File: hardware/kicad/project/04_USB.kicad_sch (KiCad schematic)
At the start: 0 parts

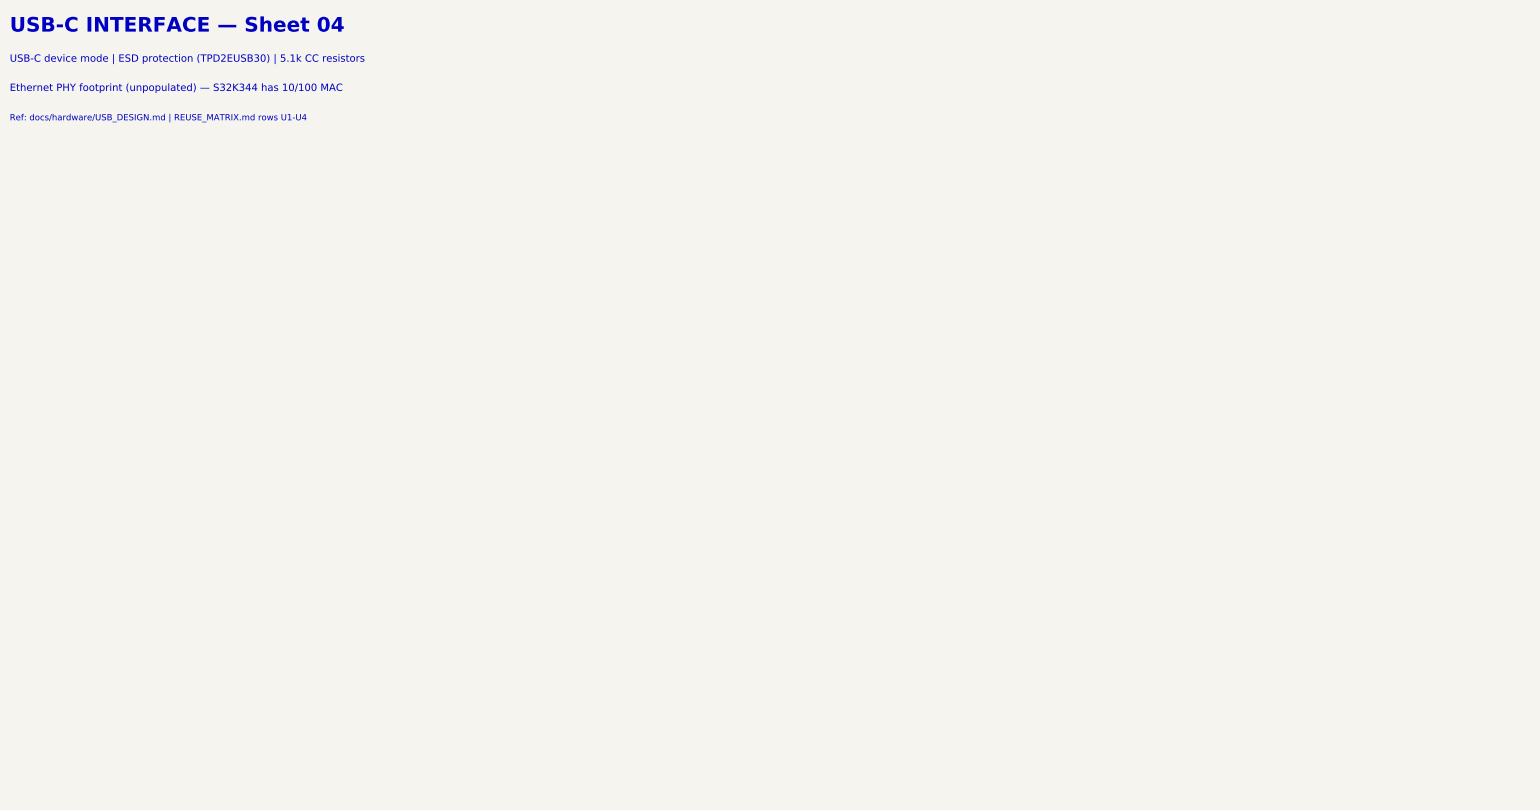
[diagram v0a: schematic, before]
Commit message: feat(hardware): TB-HW-002 — populate all 12 schematic sheets with components
Populated 235 component symbols across all 12 KiCad schematic sheets:
- 01_Power: Reverse polarity, TVS (SMCJ33A), buck (LMR33630), LDO (TPS7A1633), VREF (REF5050) — 30 symbols
- 02_MCU: S32K344 (6 units), clock (40MHz+32kHz), decoupling, reset, boot config, LEDs — 30 symbols
- 03_CAN: 4x TJA1043 with CM chokes (ACT45B-510), split termination, bus filter caps — 36 symbols
- 04_USB: Molex USB-C, TPD2EUSB30 ESD, CC resistors, eFuse, Ethernet PHY footprint — 9 symbols
- 05_Inputs: 8 analog channels (RC+clamp), 2x CJ125 WBO2, 2x TLE2072 knock amps — 50 symbols
- 06_Injectors: TLE8888-2QK (8-ch P&H), flyback diodes, current sense — 14 symbols
- 07_Ignition: 6x ISL9V3040S3 IGBTs with gate resistors (100R), pull-downs (10k) — 24 symbols
- 08_Outputs: DRV8873 ETC H-bridge, TLE8110ED low-side (boost+relays), BTS4140N tach — 12 symbols
- 09_Protection: TPS3850G33 watchdog, safe-state FET, ESD diodes (PESD5V0) — 14 symbols
- 10_Connectors: 42-pin Deutsch DTM (2 units), 2x CAN 4-pin, diagnostic 4-pin — 5 symbols
- 11_Programming: TC2050 SWD, 8 test points, production security notes — 11 symbols
- 00_Cover: Block diagram, BOM summary, spec references, revision history

Symbol library: 18 custom symbols with complete pin assignments
Components from COMPONENT_SELECTION.md r0.1
42-pin connector per INTERFACE_SPECIFICATION.md (authority)
All MCU pins per MCU_SELECTION.md pin allocation
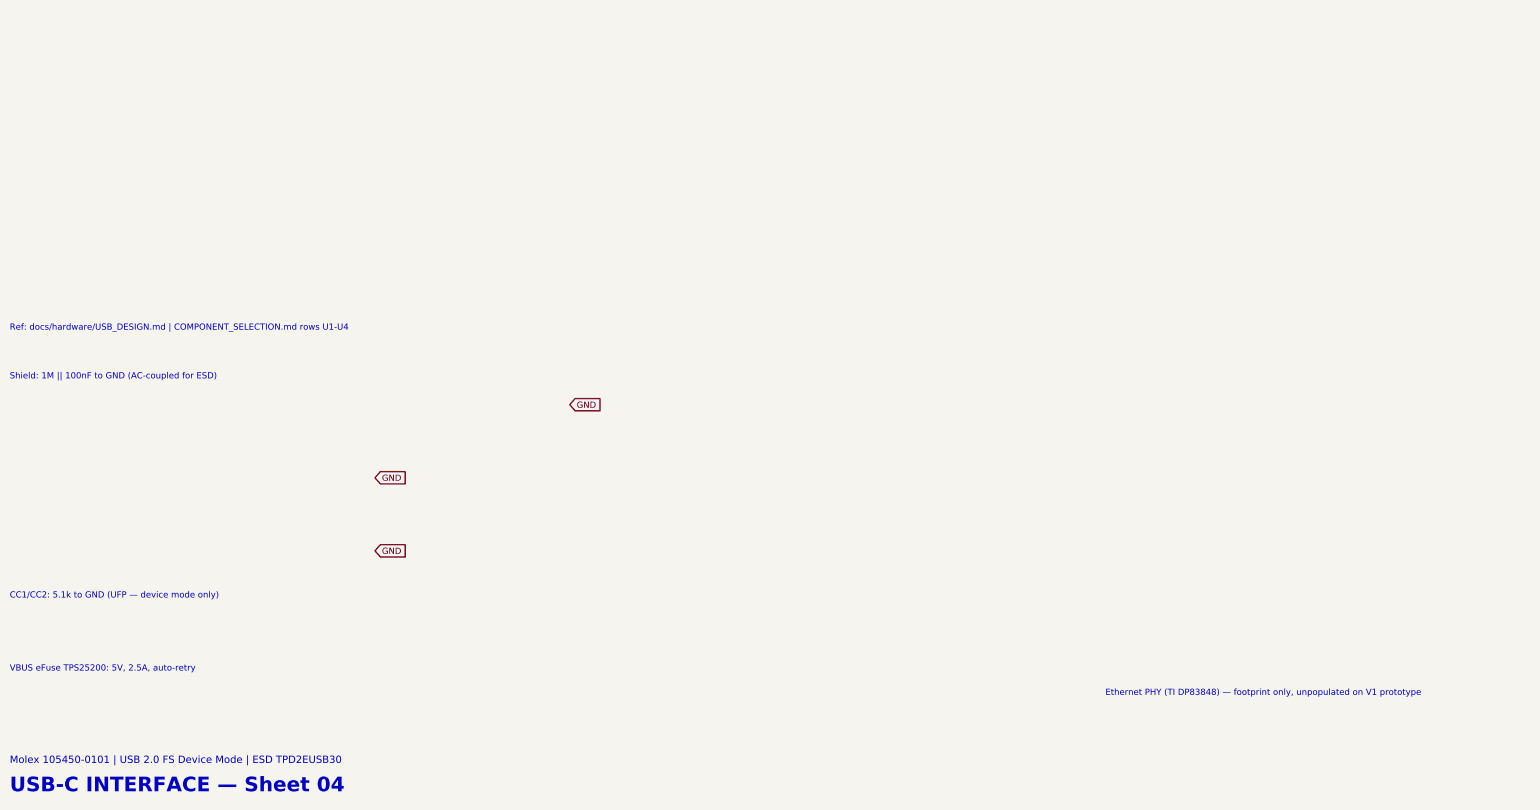
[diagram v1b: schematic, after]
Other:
- note added: "CC1/CC2: 5.1k to GND (UFP — device mode only)"
- note added: "Ethernet PHY (TI DP83848) — footprint only, unpopulated on V1 prototype"
- note added: "Molex 105450-0101 | USB 2.0 FS Device Mode | ESD TPD2EUSB30"
- note added: "Ref: docs/hardware/USB_DESIGN.md | COMPONENT_SELECTION.md rows U1-U4"
- note added: "Shield: 1M || 100nF to GND (AC-coupled for ESD)"
- note added: "VBUS eFuse TPS25200: 5V, 2.5A, auto-retry"
- note removed: "Ethernet PHY footprint (unpopulated) — S32K344 has 10/100 MAC"
- note removed: "Ref: docs/hardware/USB_DESIGN.md | REUSE_MATRIX.md rows U1-U4"
- note removed: "USB-C device mode | ESD protection (TPD2EUSB30) | 5.1k CC resistors"
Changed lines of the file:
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@@
-(kicad_sch (version 20240108) (generator "eeschema")
+(kicad_sch (version 20240108) (generator "7100CPT-schematic-gen")
   (paper "A3")
   (title_block
     (title "7100CPT ECU — USB-C Interface")
     (date "2026-07-03")
-    (rev "0.1")
+    (rev "0.2")
     (company "${COMPANY}")
-    (comment 1 "USB-C device, ESD (TPD2EUSB30), CC resistors, Ethernet PHY footprint (NP)")
+    (comment 1 "USB-C device, ESD, CC resistors, Ethernet PHY footprint (NP)")
     (comment 2 "NXP S32K344 | rusEFI Firmware | IPC Class 3")
     (comment 3 "High-Tg FR-4 (TG170+) | ENIG | 1.6 mm")
-    (comment 4 "REUSE_MATRIX.md — NXP Reference Following")
+    (comment 4 "Phase 0 Approved | REUSE_MATRIX gate passed")
     (comment 5 "-40C to +85C | IP67 Target | 6-Layer")
   )
-  (symbol_instances)
-  (text "USB-C INTERFACE — Sheet 04"
-    (at 25 24 0) (effects (font (size 3.0 3.0) bold) (justify left bottom)))
-  (text "USB-C device mode | ESD protection (TPD2EUSB30) | 5.1k CC resistors"
-    (at 25 30 0) (effects (font (size 1.5 1.5)) (justify left bottom)))
-  (text "Ethernet PHY footprint (unpopulated) — S32K344 has 10/100 MAC"
-    (at 25 36 0) (effects (font (size 1.5 1.5)) (justify left bottom)))
-  (text "Ref: docs/hardware/USB_DESIGN.md | REUSE_MATRIX.md rows U1-U4"
-    (at 25 42 0) (effects (font (size 1.27 1.27)) (justify left bottom)))
+  (symbol_instances
+  (symbol (lib_id "7100CPT:USB_C_MOLEX") (at 100 150 0) (unit 1)
+    (exclude_from_sim yes) (in_bom yes) (on_board yes) (dnp no)
+    (property "Reference" "J2" (at 100 150 0) (effects (font (size 1.27 1.27))))
+    (property "Value" "105450-0101" (at 100 143.65 0) (effects (font (size 1.27 1.27))))
+  )
+  (symbol (lib_id "7100CPT:TPD2EUSB30") (at 150 150 0) (unit 1)
+    (exclude_from_sim yes) (in_bom yes) (on_board yes) (dnp no)
+    (property "Reference" "U30" (at 150 150 0) (effects (font (size 1.27 1.27))))
+    (property "Value" "TPD2EUSB30DRTR" (at 150 143.65 0) (effects (font (size 1.27 1.27))))
+  )
+  (symbol (lib_id "Device:R") (at 100 130 0) (unit 1)
+    (exclude_from_sim yes) (in_bom yes) (on_board yes) (dnp no)
+    (property "Reference" "R16" (at 100 130 0) (effects (font (size 1.27 1.27))))
+    (property "Value" "5.1k" (at 100 123.65 0) (effects (font (size 1.27 1.27))))
+  )
+  (symbol (lib_id "Device:R") (at 100 115 0) (unit 1)
+    (exclude_from_sim yes) (in_bom yes) (on_board yes) (dnp no)
+    (property "Reference" "R17" (at 100 115 0) (effects (font (size 1.27 1.27))))
+    (property "Value" "5.1k" (at 100 108.65 0) (effects (font (size 1.27 1.27))))
+  )
+  (symbol (lib_id "Device:R") (at 130 155 0) (unit 1)
+    (exclude_from_sim yes) (in_bom yes) (on_board yes) (dnp no)
+    (property "Reference" "R18" (at 130 155 0) (effects (font (size 1.27 1.27))))
+    (property "Value" "22R" (at 130 148.65 0) (effects (font (size 1.27 1.27))))
+  )
+  (symbol (lib_id "Device:R") (at 130 145 0) (unit 1)
+    (exclude_from_sim yes) (in_bom yes) (on_board yes) (dnp no)
+    (property "Reference" "R19" (at 130 145 0) (effects (font (size 1.27 1.27))))
+    (property "Value" "22R" (at 130 138.65 0) (effects (font (size 1.27 1.27))))
+  )
+  (symbol (lib_id "Device:Fuse") (at 60 150 0) (unit 1)
+    (exclude_from_sim yes) (in_bom yes) (on_board yes) (dnp no)
+    (property "Reference" "F2" (at 60 150 0) (effects (font (size 1.27 1.27))))
+    (property "Value" "TPS25200_2.5A" (at 60 143.65 0) (effects (font (size 1.27 1.27))))
+  )
+  (symbol (lib_id "Device:R") (at 100 100 0) (unit 1)
+    (exclude_from_sim yes) (in_bom yes) (on_board yes) (dnp no)
+    (property "Reference" "R20" (at 100 100 0) (effects (font (size 1.27 1.27))))
+    (property "Value" "1M" (at 100 93.65 0) (effects (font (size 1.27 1.27))))
+  )
+  (symbol (lib_id "Device:C") (at 120 100 0) (unit 1)
+    (exclude_from_sim yes) (in_bom yes) (on_board yes) (dnp no)
+    (property "Reference" "C34" (at 120 100 0) (effects (font (size 1.27 1.27))))
+    (property "Value" "100nF_50V_X7R" (at 120 93.65 0) (effects (font (size 1.27 1.27))))
+  )
+  )
+  (text "USB-C INTERFACE — Sheet 04" (at 25 180 0) (effects (font (size 3.0 3.0) bold) (justify left bottom)))
+  (text "Molex 105450-0101 | USB 2.0 FS Device Mode | ESD TPD2EUSB30" (at 25 174 0) (effects (font (size 1.5 1.5)) (justify left bottom)))
+  (text "CC1/CC2: 5.1k to GND (UFP — device mode only)" (at 25 140 0) (effects (font (size 1.27 1.27)) (justify left bottom)))
+  (text "Shield: 1M || 100nF to GND (AC-coupled for ESD)" (at 25 95 0) (effects (font (size 1.27 1.27)) (justify left bottom)))
+  (text "VBUS eFuse TPS25200: 5V, 2.5A, auto-retry" (at 25 155 0) (effects (font (size 1.27 1.27)) (justify left bottom)))
+  (text "Ref: docs/hardware/USB_DESIGN.md | COMPONENT_SELECTION.md rows U1-U4" (at 25 85 0) (effects (font (size 1.27 1.27)) (justify left bottom)))
+  (text "Ethernet PHY (TI DP83848) — footprint only, unpopulated on V1 prototype" (at 250 160 0) (effects (font (size 1.27 1.27)) (justify left bottom)))
+  (global_label "GND" (shape input) (at 140 100 0) (effects (font (size 1.27 1.27))))
+  (global_label "GND" (shape input) (at 100 130 0) (effects (font (size 1.27 1.27))))
+  (global_label "GND" (shape input) (at 100 115 0) (effects (font (size 1.27 1.27))))
   (sheet_instances
     (path "/04_usb/" (page "5"))
